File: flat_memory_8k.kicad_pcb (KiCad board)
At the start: 2 copper layers, 85 x 65 mm, 37 parts, among them X1 Power, X2 Address, X3 Data, X4 Mode, X5 Control, X6 Clock

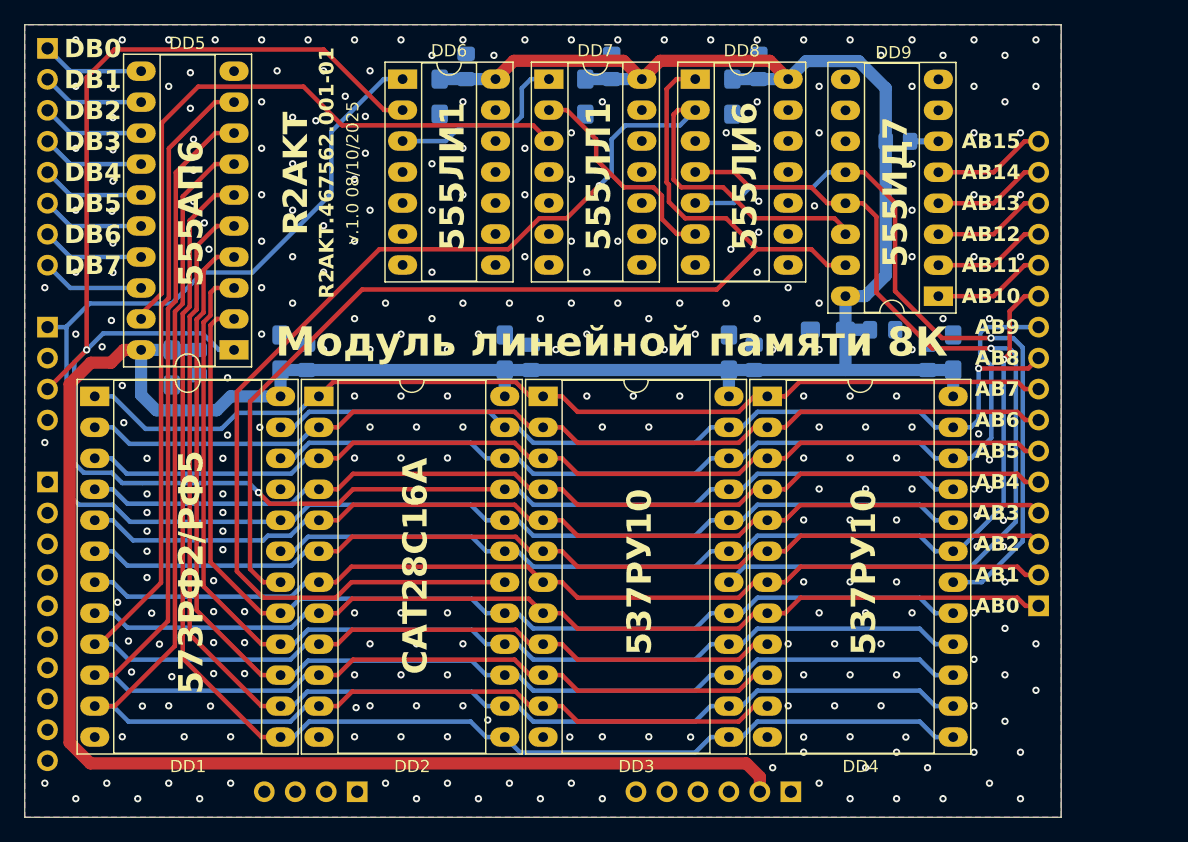
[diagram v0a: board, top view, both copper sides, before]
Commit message: Add files via upload
Add optional footprint for memory
Добавлены опциональные посадочные места памяти
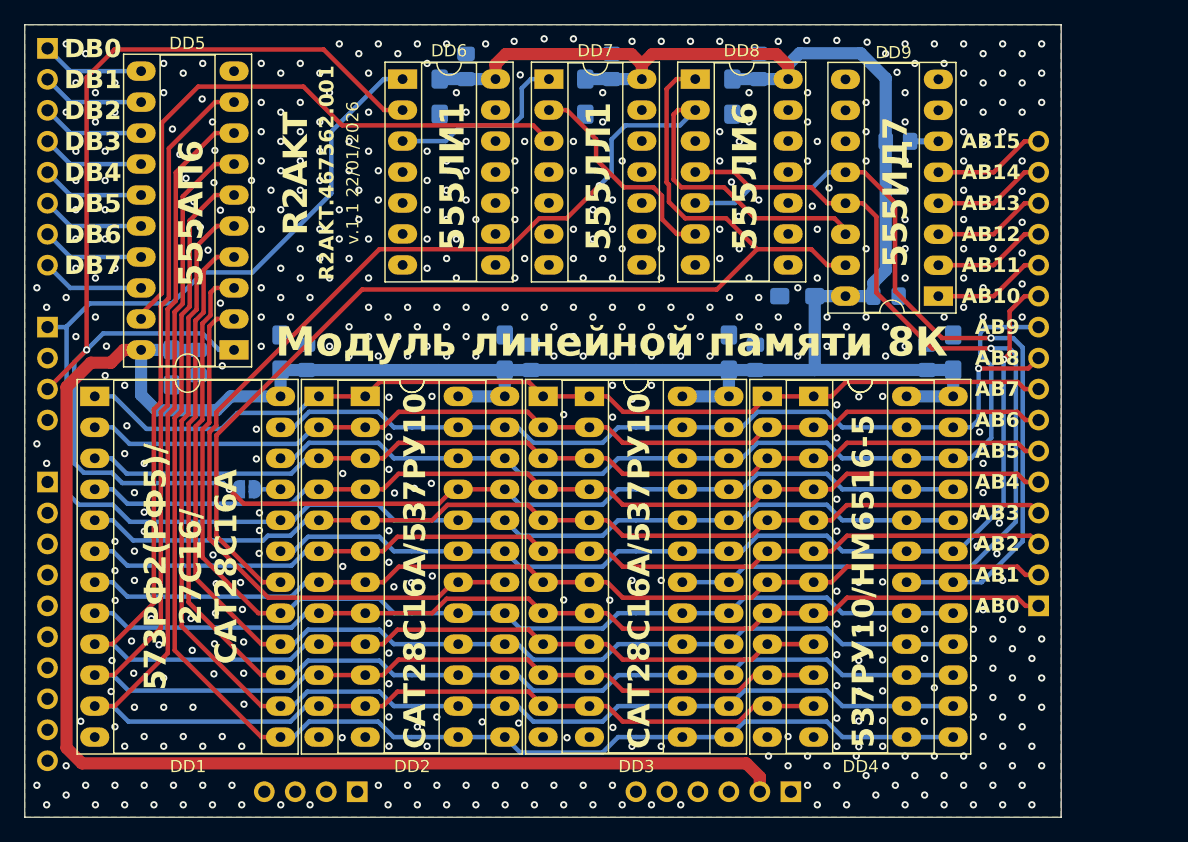
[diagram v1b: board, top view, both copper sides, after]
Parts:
- added DD10: DUAL SOCKET, Package_DIP:DIP-24_W7.62mm_LongPads, F.Cu at (96.8, 109.6)
- added DD11: DUAL SOCKET, Package_DIP:DIP-24_W7.62mm_LongPads, F.Cu at (115.1, 109.6)
- added DD12: DUAL SOCKET, Package_DIP:DIP-24_W7.62mm_LongPads, F.Cu at (133.5, 109.6)
- added JP1: Jumper_2_Open, Jumper:SolderJumper-2_P1.3mm_Open_RoundedPad1.0x1.5mm, B.Cu at (87.1, 117.2)
- moved REF** 42.1 mm to (149.0, 83.1)
- moved REF** 18.4 mm to (83.0, 123.6)
- moved C12 3.73 mm to (132.2, 101.4)
- moved C11 2.77 mm to (139.5, 101.4)
- moved C5 0.10 mm to (128.8, 106.4)
- moved C7 0.05 mm to (142.8, 106.4)
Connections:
- DD1 pad 21: unconnected-(DD1-Vpp-Pad21) -> Net-(DD1-Vpp)
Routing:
- net +5: track 257.3 -> 274.6 mm
- net /DATA_B0: track 108.6 -> 113.0 mm
- net /~{6K_CS}: track 75.3 -> 79.1 mm
- net /~{8K_CS}: track 60.9 -> 64.8 mm
- net /DATA_B2: track 109.3 -> 113.1 mm
- net /DATA_B1: track 109.3 -> 113.1 mm
- net Net-(DD1-Vpp): track 0.00 -> 2.42 mm
- net /~{2K_CS}: track 92.1 -> 94.4 mm
- net /~{4K_CS}: track 110.4 -> 112.0 mm
- net /~{MEMW}: track 155.2 -> 156.0 mm
- net /DATA_B7: track 87.3 -> 88.0 mm
- net /DATA_B6: track 92.9 -> 93.5 mm
- net /DATA_B4: track 104.0 -> 104.5 mm
- net /DATA_B5: track 98.4 -> 99.0 mm
- net /DATA_B3: track 109.7 -> 110.2 mm
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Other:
- board text added: "537РУ10/HM6516-5"
- board text added: "573РФ2(РФ5)/ 27C16/ CAT28C16A"
- board text added: "CAT28C16A/537РУ10"
- board text added: "R2AKT.467562.001"
- board text added: "v.1.1 22/01/2026"
- board text removed: "537РУ10"
- board text removed: "573РФ2/РФ5"
- board text removed: "CAT28C16A"
- board text removed: "R2AKT.467562.001-01"
- board text removed: "v.1.0 08/10/2025"

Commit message: Update
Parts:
- added C13: 100n, Capacitor_SMD:C_0805_2012Metric_Pad1.18x1.45mm_HandSolder, B.Cu at (147.1, 88.7)
- moved REF** 0.34 mm to (149.2, 82.8)
- renumbered C13 to C14, C14 to C15, C15 to C16, C16 to C17, C17 to C18, C18 to C19
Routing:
- net Net-(DD9-E3): track 2.32 -> 4.61 mm

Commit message: Fix silk
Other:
- board text added: "R2AKT.467522.001"
- board text removed: "R2AKT.467562.001"
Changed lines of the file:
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@@
 		(date "2026-03-10")
 		(company "R2AKT")
-		(comment 1 "R2AKT.467562.001")
+		(comment 1 "R2AKT.467522.001")
 		(comment 2 "R2AKT")
 	)
@@
 		)
 	)
-	(gr_text "R2AKT.467562.001"
+	(gr_text "R2AKT.467522.001"
 		(at 93.5986 91.296972 90)
 		(layer "F.SilkS")
